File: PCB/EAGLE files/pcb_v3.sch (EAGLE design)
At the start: 10 parts

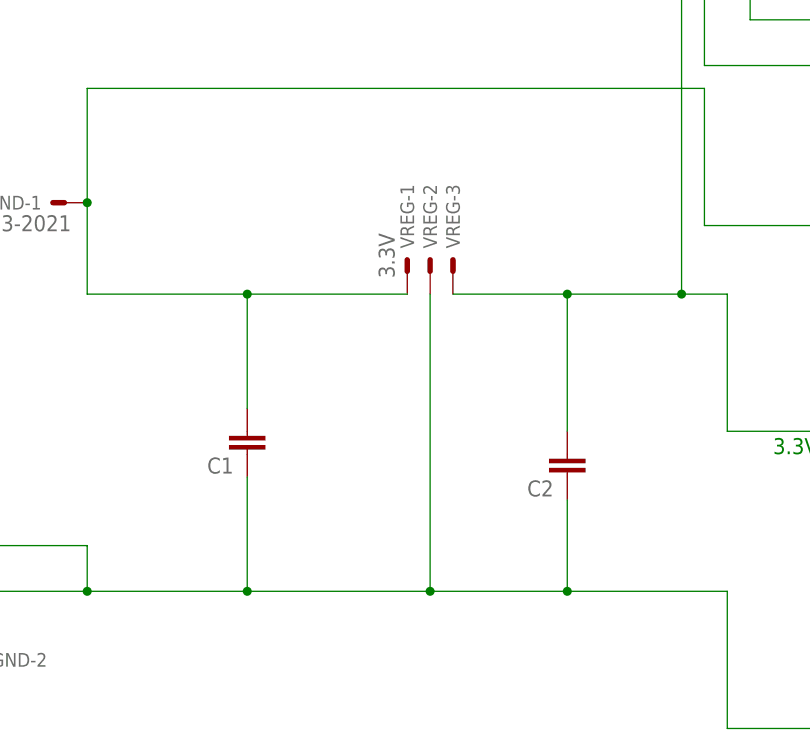
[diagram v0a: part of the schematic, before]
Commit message: PCB with new VR ready for print
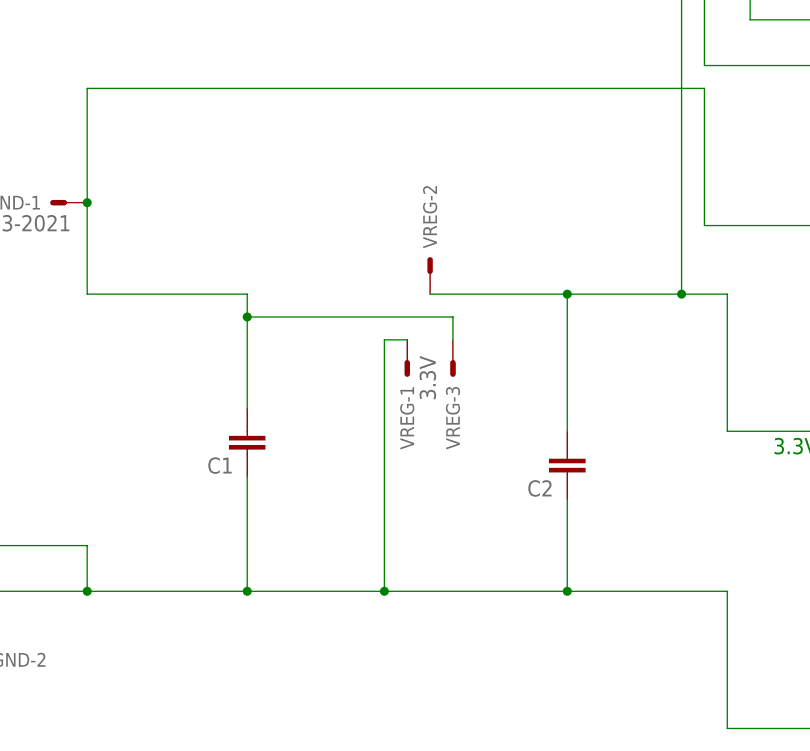
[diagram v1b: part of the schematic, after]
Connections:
- net N$12: now also VREG-1.S; no longer VREG-2.S
- net N$14: now also VREG-3.S; no longer VREG-1.S
- net N$4: now also VREG-2.S; no longer VREG-3.S
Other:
- moved on the sheet: VREG-1, VREG-3
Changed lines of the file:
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@@
 <instance part="VCC-GND" gate="-1" x="-20.32" y="71.12" rot="R180"/>
 <instance part="VCC-GND" gate="-2" x="-35.56" y="20.32"/>
-<instance part="VREG" gate="-1" x="17.78" y="63.5" rot="R90"/>
+<instance part="VREG" gate="-1" x="17.78" y="53.34" rot="R270"/>
 <instance part="VREG" gate="-2" x="20.32" y="63.5" rot="R90"/>
-<instance part="VREG" gate="-3" x="22.86" y="63.5" rot="R90"/>
+<instance part="VREG" gate="-3" x="22.86" y="53.34" rot="R270"/>
 </instances>
 <busses>
@@
 <wire x1="17.78" y1="129.54" x2="17.78" y2="93.98" width="0.1524" layer="91"/>
 <wire x1="17.78" y1="93.98" x2="48.26" y2="93.98" width="0.1524" layer="91"/>
-<wire x1="22.86" y1="60.96" x2="35.56" y2="60.96" width="0.1524" layer="91"/>
 <wire x1="35.56" y1="60.96" x2="48.26" y2="60.96" width="0.1524" layer="91"/>
 <wire x1="48.26" y1="60.96" x2="53.34" y2="60.96" width="0.1524" layer="91"/>
@@
 <pinref part="C2" gate="G$1" pin="2"/>
 <wire x1="35.56" y1="45.72" x2="35.56" y2="60.96" width="0.1524" layer="91"/>
+<pinref part="VREG" gate="-2" pin="S"/>
+<wire x1="20.32" y1="60.96" x2="35.56" y2="60.96" width="0.1524" layer="91"/>
 <junction x="35.56" y="60.96"/>
-<pinref part="VREG" gate="-3" pin="S"/>
 </segment>
 </net>
@@
 <wire x1="-38.1" y1="27.94" x2="-17.78" y2="27.94" width="0.1524" layer="91"/>
 <wire x1="-17.78" y1="27.94" x2="0" y2="27.94" width="0.1524" layer="91"/>
-<wire x1="0" y1="27.94" x2="20.32" y2="27.94" width="0.1524" layer="91"/>
-<wire x1="20.32" y1="27.94" x2="35.56" y2="27.94" width="0.1524" layer="91"/>
+<wire x1="0" y1="27.94" x2="15.24" y2="27.94" width="0.1524" layer="91"/>
+<wire x1="15.24" y1="27.94" x2="35.56" y2="27.94" width="0.1524" layer="91"/>
 <wire x1="35.56" y1="27.94" x2="53.34" y2="27.94" width="0.1524" layer="91"/>
 <wire x1="53.34" y1="27.94" x2="53.34" y2="12.7" width="0.1524" layer="91"/>
@@
 <wire x1="0" y1="40.64" x2="0" y2="27.94" width="0.1524" layer="91"/>
 <junction x="0" y="27.94"/>
-<wire x1="20.32" y1="60.96" x2="20.32" y2="27.94" width="0.1524" layer="91"/>
-<junction x="20.32" y="27.94"/>
-<pinref part="VREG" gate="-2" pin="S"/>
+<pinref part="VREG" gate="-1" pin="S"/>
+<wire x1="17.78" y1="55.88" x2="15.24" y2="55.88" width="0.1524" layer="91"/>
+<wire x1="15.24" y1="55.88" x2="15.24" y2="27.94" width="0.1524" layer="91"/>
+<junction x="15.24" y="27.94"/>
 </segment>
 </net>
@@
 <wire x1="-17.78" y1="60.96" x2="-17.78" y2="71.12" width="0.1524" layer="91"/>
 <wire x1="-17.78" y1="71.12" x2="-17.78" y2="83.82" width="0.1524" layer="91"/>
-<wire x1="17.78" y1="60.96" x2="0" y2="60.96" width="0.1524" layer="91"/>
 <pinref part="H-BRIDGE" gate="A" pin="4"/>
 <wire x1="0" y1="60.96" x2="-17.78" y2="60.96" width="0.1524" layer="91"/>
@@
 <junction x="-17.78" y="71.12"/>
 <pinref part="C1" gate="G$1" pin="2"/>
-<wire x1="0" y1="48.26" x2="0" y2="60.96" width="0.1524" layer="91"/>
-<junction x="0" y="60.96"/>
-<pinref part="VREG" gate="-1" pin="S"/>
+<wire x1="0" y1="48.26" x2="0" y2="58.42" width="0.1524" layer="91"/>
+<pinref part="VREG" gate="-3" pin="S"/>
+<wire x1="0" y1="58.42" x2="0" y2="60.96" width="0.1524" layer="91"/>
+<wire x1="22.86" y1="55.88" x2="22.86" y2="58.42" width="0.1524" layer="91"/>
+<wire x1="22.86" y1="58.42" x2="0" y2="58.42" width="0.1524" layer="91"/>
+<junction x="0" y="58.42"/>
 </segment>
 </net>

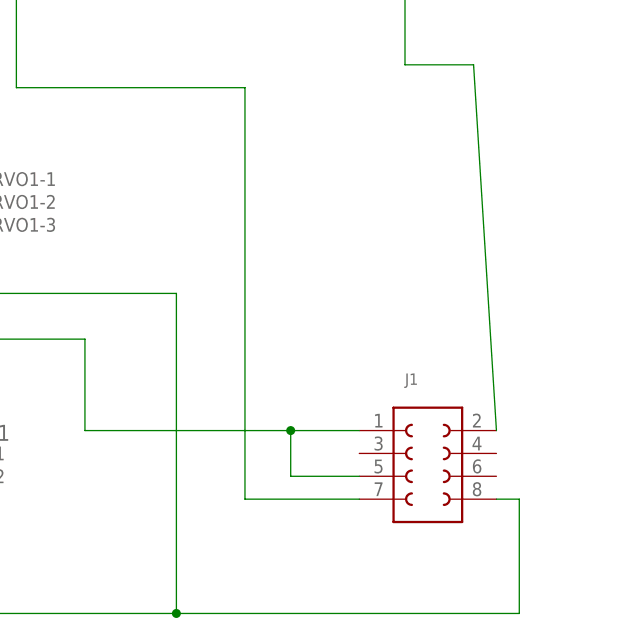
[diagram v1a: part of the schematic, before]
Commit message: Add second ESP8266 to PCB
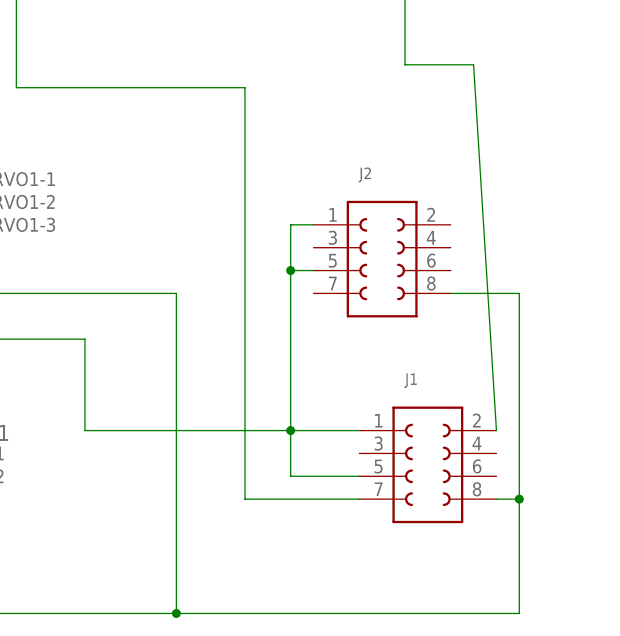
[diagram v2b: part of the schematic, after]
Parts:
- added J2: (no value), Board-to-Board (rev17e):61300821121
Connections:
- net N$12: now also J2.5
- net N$4: now also J2.1, J2.3
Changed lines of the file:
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@@
 <part name="VCC-GND" library="con-molex" deviceset="22-23-2021" device=""/>
 <part name="VREG" library="con-molex" deviceset="22-23-2031" device="" value="3.3V"/>
+<part name="J2" library="Board-to-Board (rev17e)" deviceset="61300821121" device=""/>
 </parts>
 <sheets>
@@
 <instance part="VREG" gate="-2" x="20.32" y="63.5" rot="R90"/>
 <instance part="VREG" gate="-3" x="22.86" y="53.34" rot="R270"/>
+<instance part="J2" gate="G$1" x="200.66" y="53.34"/>
 </instances>
 <busses>
@@
 <wire x1="20.32" y1="60.96" x2="35.56" y2="60.96" width="0.1524" layer="91"/>
 <junction x="35.56" y="60.96"/>
+<pinref part="J2" gate="G$1" pin="1"/>
+<wire x1="193.04" y1="55.88" x2="190.5" y2="55.88" width="0.1524" layer="91"/>
+<wire x1="190.5" y1="55.88" x2="190.5" y2="50.8" width="0.1524" layer="91"/>
+<pinref part="J2" gate="G$1" pin="3"/>
+<wire x1="190.5" y1="50.8" x2="190.5" y2="33.02" width="0.1524" layer="91"/>
+<wire x1="193.04" y1="50.8" x2="190.5" y2="50.8" width="0.1524" layer="91"/>
+<junction x="190.5" y="50.8"/>
 </segment>
 </net>
@@
 <wire x1="15.24" y1="55.88" x2="15.24" y2="27.94" width="0.1524" layer="91"/>
 <junction x="15.24" y="27.94"/>
-</segment>
-</net>
+<pinref part="J2" gate="G$1" pin="5"/>
+<wire x1="208.28" y1="48.26" x2="215.9" y2="48.26" width="0.1524" layer="91"/>
+<wire x1="215.9" y1="48.26" x2="215.9" y2="25.4" width="0.1524" layer="91"/>
+<junction x="215.9" y="25.4"/>
+</segment>
+</net>
